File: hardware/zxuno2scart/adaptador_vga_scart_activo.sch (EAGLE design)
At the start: 13 parts, among them T1 2N3904, T2 2N3904, T3 2N3904

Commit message: 
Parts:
- C1, C3: device capacitor-wima:C5/3.5 -> capacitor-wima:C2,5-3
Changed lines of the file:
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@@
 <?xml version="1.0" encoding="utf-8"?>
 <!DOCTYPE eagle SYSTEM "eagle.dtd">
-<eagle version="6.5.0">
+<eagle version="7.3.0">
 <drawing>
 <settings>
@@
 <grid distance="0.1" unitdist="inch" unit="inch" style="lines" multiple="1" display="no" altdistance="0.01" altunitdist="inch" altunit="inch"/>
 <layers>
-<layer number="1" name="Top" color="4" fill="1" visible="no" active="no"/>
-<layer number="2" name="Route2" color="1" fill="3" visible="no" active="no"/>
-<layer number="3" name="Route3" color="4" fill="3" visible="no" active="no"/>
-<layer number="4" name="Route4" color="1" fill="4" visible="no" active="no"/>
-<layer number="5" name="Route5" color="4" fill="4" visible="no" active="no"/>
-<layer number="6" name="Route6" color="1" fill="8" visible="no" active="no"/>
-<layer number="7" name="Route7" color="4" fill="8" visible="no" active="no"/>
-<layer number="8" name="Route8" color="1" fill="2" visible="no" active="no"/>
-<layer number="9" name="Route9" color="4" fill="2" visible="no" active="no"/>
-<layer number="10" name="Route10" color="1" fill="7" visible="no" active="no"/>
-<layer number="11" name="Route11" color="4" fill="7" visible="no" active="no"/>
-<layer number="12" name="Route12" color="1" fill="5" visible="no" active="no"/>
-<layer number="13" name="Route13" color="4" fill="5" visible="no" active="no"/>
-<layer number="14" name="Route14" color="1" fill="6" visible="no" active="no"/>
-<layer number="15" name="Route15" color="4" fill="6" visible="no" active="no"/>
-<layer number="16" name="Bottom" color="1" fill="1" visible="no" active="no"/>
-<layer number="17" name="Pads" color="2" fill="1" visible="no" active="no"/>
-<layer number="18" name="Vias" color="2" fill="1" visible="no" active="no"/>
-<layer number="19" name="Unrouted" color="6" fill="1" visible="no" active="no"/>
-<layer number="20" name="Dimension" color="15" fill="1" visible="no" active="no"/>
-<layer number="21" name="tPlace" color="7" fill="1" visible="no" active="no"/>
-<layer number="22" name="bPlace" color="7" fill="1" visible="no" active="no"/>
-<layer number="23" name="tOrigins" color="15" fill="1" visible="no" active="no"/>
-<layer number="24" name="bOrigins" color="15" fill="1" visible="no" active="no"/>
-<layer number="25" name="tNames" color="7" fill="1" visible="no" active="no"/>
-<layer number="26" name="bNames" color="7" fill="1" visible="no" active="no"/>
-<layer number="27" name="tValues" color="7" fill="1" visible="no" active="no"/>
-<layer number="28" name="bValues" color="7" fill="1" visible="no" active="no"/>
+<layer number="1" name="Top" color="4" fill="1" visible="yes" active="no"/>
+<layer number="2" name="Route2" color="1" fill="3" visible="yes" active="no"/>
+<layer number="3" name="Route3" color="4" fill="3" visible="yes" active="no"/>
+<layer number="4" name="Route4" color="1" fill="4" visible="yes" active="no"/>
+<layer number="5" name="Route5" color="4" fill="4" visible="yes" active="no"/>
+<layer number="6" name="Route6" color="1" fill="8" visible="yes" active="no"/>
+<layer number="7" name="Route7" color="4" fill="8" visible="yes" active="no"/>
+<layer number="8" name="Route8" color="1" fill="2" visible="yes" active="no"/>
+<layer number="9" name="Route9" color="4" fill="2" visible="yes" active="no"/>
+<layer number="10" name="Route10" color="1" fill="7" visible="yes" active="no"/>
+<layer number="11" name="Route11" color="4" fill="7" visible="yes" active="no"/>
+<layer number="12" name="Route12" color="1" fill="5" visible="yes" active="no"/>
+<layer number="13" name="Route13" color="4" fill="5" visible="yes" active="no"/>
+<layer number="14" name="Route14" color="1" fill="6" visible="yes" active="no"/>
+<layer number="15" name="Route15" color="4" fill="6" visible="yes" active="no"/>
+<layer number="16" name="Bottom" color="1" fill="1" visible="yes" active="no"/>
+<layer number="17" name="Pads" color="2" fill="1" visible="yes" active="no"/>
+<layer number="18" name="Vias" color="2" fill="1" visible="yes" active="no"/>
+<layer number="19" name="Unrouted" color="6" fill="1" visible="yes" active="no"/>
+<layer number="20" name="Dimension" color="15" fill="1" visible="yes" active="no"/>
+<layer number="21" name="tPlace" color="7" fill="1" visible="yes" active="no"/>
+<layer number="22" name="bPlace" color="7" fill="1" visible="yes" active="no"/>
+<layer number="23" name="tOrigins" color="15" fill="1" visible="yes" active="no"/>
+<layer number="24" name="bOrigins" color="15" fill="1" visible="yes" active="no"/>
+<layer number="25" name="tNames" color="7" fill="1" visible="yes" active="no"/>
+<layer number="26" name="bNames" color="7" fill="1" visible="yes" active="no"/>
+<layer number="27" name="tValues" color="7" fill="1" visible="yes" active="no"/>
+<layer number="28" name="bValues" color="7" fill="1" visible="yes" active="no"/>
 <layer number="29" name="tStop" color="7" fill="3" visible="no" active="no"/>
 <layer number="30" name="bStop" color="7" fill="6" visible="no" active="no"/>
@@
 <layer number="35" name="tGlue" color="7" fill="4" visible="no" active="no"/>
 <layer number="36" name="bGlue" color="7" fill="5" visible="no" active="no"/>
-<layer number="37" name="tTest" color="7" fill="1" visible="no" active="no"/>
-<layer number="38" name="bTest" color="7" fill="1" visible="no" active="no"/>
+<layer number="37" name="tTest" color="7" fill="1" visible="yes" active="no"/>
+<layer number="38" name="bTest" color="7" fill="1" visible="yes" active="no"/>
 <layer number="39" name="tKeepout" color="4" fill="11" visible="no" active="no"/>
 <layer number="40" name="bKeepout" color="1" fill="11" visible="no" active="no"/>
@@
 <layer number="44" name="Drills" color="7" fill="1" visible="no" active="no"/>
 <layer number="45" name="Holes" color="7" fill="1" visible="no" active="no"/>
-<layer number="46" name="Milling" color="3" fill="1" visible="no" active="no"/>
-<layer number="47" name="Measures" color="7" fill="1" visible="no" active="no"/>
-<layer number="48" name="Document" color="7" fill="1" visible="no" active="no"/>
-<layer number="49" name="Reference" color="7" fill="1" visible="no" active="no"/>
-<layer number="50" name="dxf" color="7" fill="1" visible="no" active="no"/>
-<layer number="51" name="tDocu" color="7" fill="1" visible="no" active="no"/>
-<layer number="52" name="bDocu" color="7" fill="1" visible="no" active="no"/>
-<layer number="53" name="tGND_GNDA" color="7" fill="1" visible="no" active="no"/>
-<layer number="54" name="bGND_GNDA" color="7" fill="1" visible="no" active="no"/>
-<layer number="56" name="wert" color="7" fill="1" visible="no" active="no"/>
-<layer number="57" name="tCAD" color="7" fill="1" visible="no" active="no"/>
+<layer number="46" name="Milling" color="3" fill="1" visible="yes" active="no"/>
+<layer number="47" name="Measures" color="7" fill="1" visible="yes" active="no"/>
+<layer number="48" name="Document" color="7" fill="1" visible="yes" active="no"/>
+<layer number="49" name="Reference" color="7" fill="1" visible="yes" active="no"/>
+<layer number="50" name="dxf" color="7" fill="1" visible="yes" active="no"/>
+<layer number="51" name="tDocu" color="7" fill="1" visible="yes" active="no"/>
+<layer number="52" name="bDocu" color="7" fill="1" visible="yes" active="no"/>
+<layer number="53" name="tGND_GNDA" color="7" fill="1" visible="yes" active="no"/>
+<layer number="54" name="bGND_GNDA" color="7" fill="1" visible="yes" active="no"/>
+<layer number="56" name="wert" color="7" fill="1" visible="yes" active="no"/>
+<layer number="57" name="tCAD" color="7" fill="1" visible="yes" active="no"/>
 <layer number="90" name="Modules" color="7" fill="1" visible="yes" active="yes"/>
 <layer number="91" name="Nets" color="2" fill="1" visible="yes" active="yes"/>
@@
 <part name="L1" library="inductors" deviceset="BL0" device="1RN1A"/>
 <part name="P+1" library="supply1" deviceset="VCC" device=""/>
-<part name="C1" library="capacitor-wima" deviceset="C" device="5/3.5"/>
+<part name="C1" library="capacitor-wima" deviceset="C" device="2,5-3"/>
 <part name="C2" library="capacitor-wima" deviceset="C" device="5/3.5"/>
-<part name="C3" library="capacitor-wima" deviceset="C" device="5/3.5"/>
+<part name="C3" library="capacitor-wima" deviceset="C" device="2,5-3"/>
 <part name="GND3" library="supply1" deviceset="GND" device=""/>
 <part name="GND4" library="supply1" deviceset="GND" device=""/>

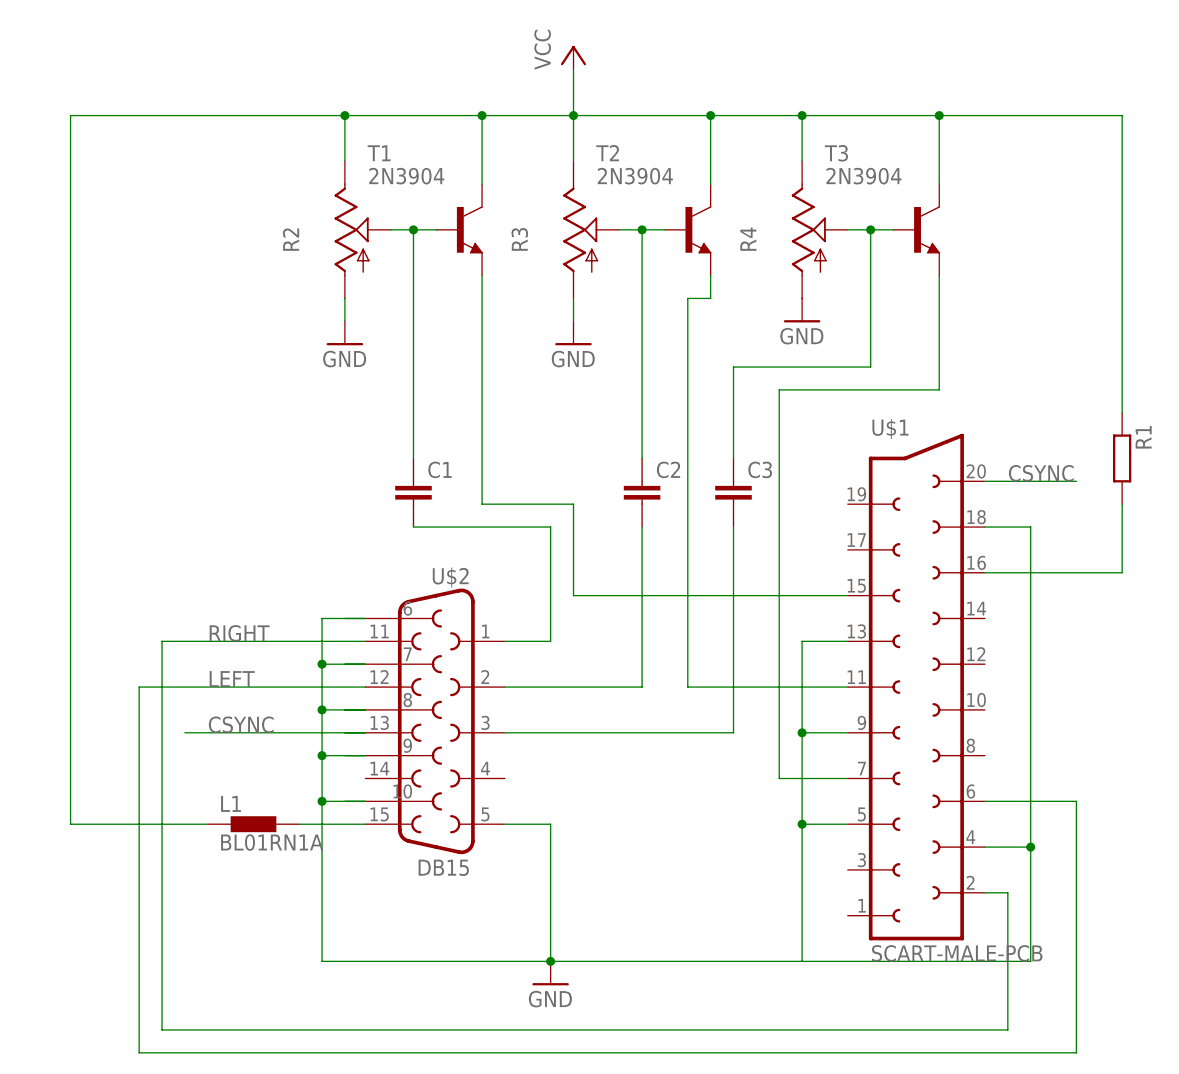
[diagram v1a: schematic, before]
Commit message: 
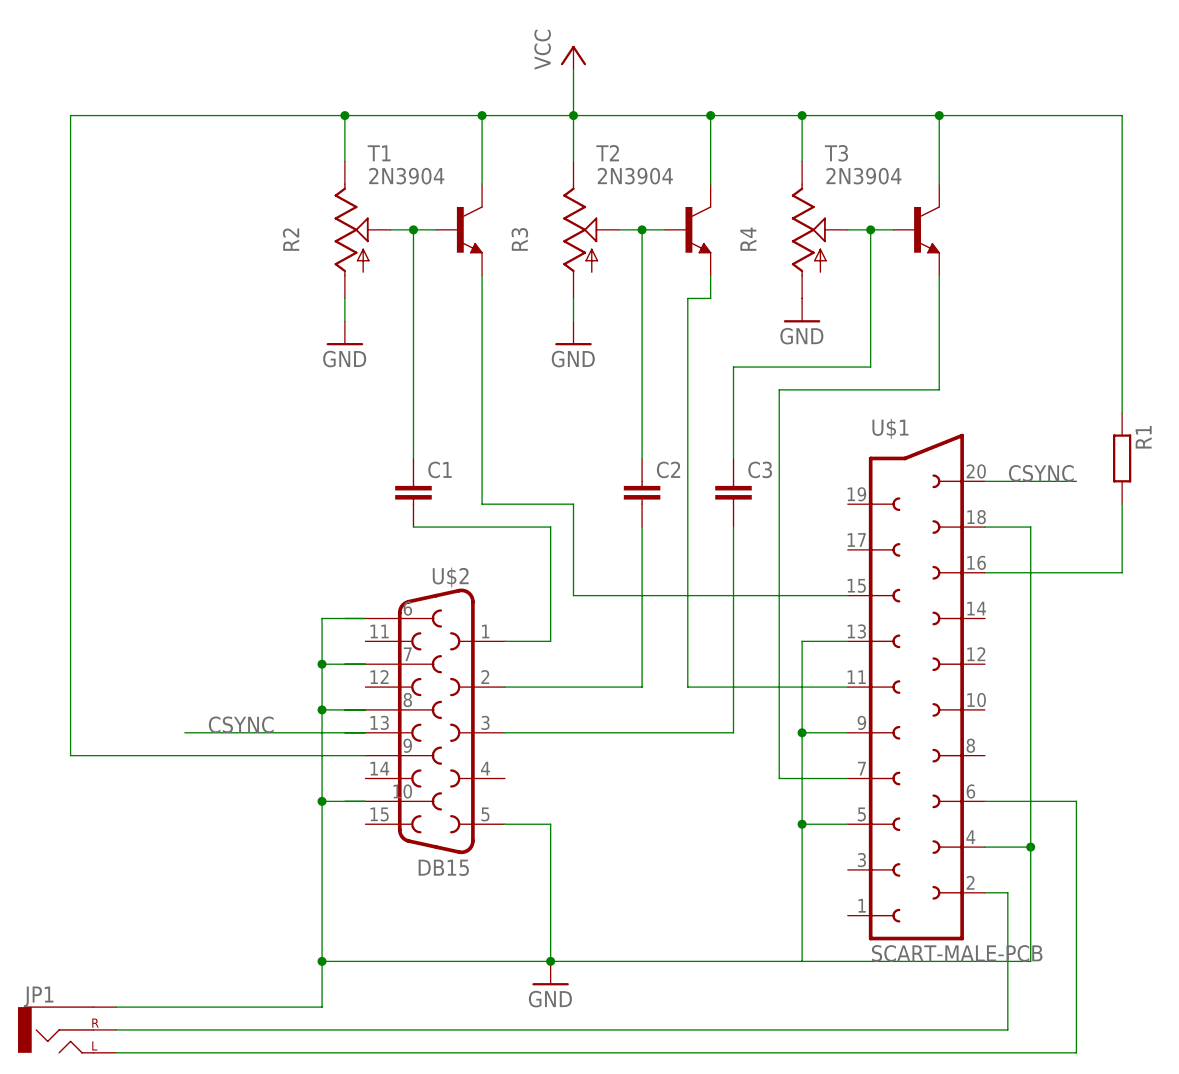
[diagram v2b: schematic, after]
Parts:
- removed L1: BL01RN1A, inductors:BL01RN1A
- added JP1: (no value), SparkFun-Connectors:AUDIO-JACKPTH
- C2: device capacitor-wima:C5/3.5 -> capacitor-wima:C2,5-3
- R1: device rcl:R-EU_0204/7 -> rcl:R-EU_0204/5
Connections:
- removed net N$2: L1.2, U$2.15
- net GND: now also JP1.SLEEVE; no longer U$2.9
- net LEFT: now also JP1.LEFT; no longer U$2.12
- net RIGHT: now also JP1.RIGHT; no longer U$2.11
- net VCC: now also U$2.9; no longer L1.1
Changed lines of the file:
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@@
 <layer number="113" name="IDFDebug" color="4" fill="1" visible="yes" active="yes"/>
 <layer number="116" name="Patch_BOT" color="7" fill="1" visible="yes" active="yes"/>
+<layer number="118" name="Rect_Pads" color="7" fill="1" visible="yes" active="yes"/>
 <layer number="121" name="_tsilk" color="7" fill="1" visible="yes" active="yes"/>
 <layer number="122" name="_bsilk" color="7" fill="1" visible="yes" active="yes"/>
@@
 <layer number="127" name="_tValues" color="7" fill="1" visible="yes" active="yes"/>
 <layer number="128" name="_bValues" color="7" fill="1" visible="yes" active="yes"/>
+<layer number="130" name="tSilk" color="7" fill="1" visible="yes" active="yes"/>
 <layer number="131" name="tAdjust" color="7" fill="1" visible="yes" active="yes"/>
 <layer number="132" name="bAdjust" color="7" fill="1" visible="yes" active="yes"/>
+<layer number="133" name="Ports" color="7" fill="1" visible="yes" active="yes"/>
+<layer number="134" name="Port2" color="7" fill="1" visible="yes" active="yes"/>
+<layer number="135" name="Port3" color="7" fill="1" visible="yes" active="yes"/>
 <layer number="144" name="Drill_legend" color="7" fill="1" visible="yes" active="yes"/>
 <layer number="150" name="Notes" color="7" fill="1" visible="yes" active="yes"/>
@@
 <layer number="223" name="223bmp" color="7" fill="1" visible="yes" active="yes"/>
 <layer number="224" name="224bmp" color="7" fill="1" visible="yes" active="yes"/>
+<layer number="231" name="Eagle3D_PG1" color="7" fill="1" visible="yes" active="yes"/>
+<layer number="232" name="Eagle3D_PG2" color="7" fill="1" visible="yes" active="yes"/>
+<layer number="233" name="Eagle3D_PG3" color="7" fill="1" visible="yes" active="yes"/>
 <layer number="248" name="Housing" color="7" fill="1" visible="yes" active="yes"/>
 <layer number="249" name="Edge" color="7" fill="1" visible="yes" active="yes"/>
@@
 <part name="U$1" library="con-hirschmann" deviceset="SCART-MALE-PCB" device=""/>
 <part name="U$2" library="SparkFun-Connectors" deviceset="DB15" device=""/>
-<part name="R1" library="rcl" deviceset="R-EU_" device="0204/7"/>
+<part name="R1" library="rcl" deviceset="R-EU_" device="0204/5"/>
 <part name="T1" library="transistor" deviceset="2N3904" device=""/>
 <part name="T2" library="transistor" deviceset="2N3904" device=""/>
@@
 <part name="GND1" library="supply1" deviceset="GND" device=""/>
 <part name="GND2" library="supply1" deviceset="GND" device=""/>
-<part name="L1" library="inductors" deviceset="BL0" device="1RN1A"/>
 <part name="P+1" library="supply1" deviceset="VCC" device=""/>
 <part name="C1" library="capacitor-wima" deviceset="C" device="2,5-3"/>
-<part name="C2" library="capacitor-wima" deviceset="C" device="5/3.5"/>
+<part name="C2" library="capacitor-wima" deviceset="C" device="2,5-3"/>
 <part name="C3" library="capacitor-wima" deviceset="C" device="2,5-3"/>
 <part name="GND3" library="supply1" deviceset="GND" device=""/>
@@
 <part name="R3" library="pot" deviceset="TRIM_US-" device="CA6V"/>
 <part name="R4" library="pot" deviceset="TRIM_US-" device="CA6V"/>
+<part name="JP1" library="SparkFun-Connectors" deviceset="AUDIO-JACK" device="PTH"/>
 </parts>
 <sheets>
@@
 <instance part="GND1" gate="1" x="-15.24" y="17.78"/>
 <instance part="GND2" gate="1" x="-12.7" y="88.9"/>
-<instance part="L1" gate="G$1" x="-48.26" y="35.56"/>
 <instance part="P+1" gate="VCC" x="-12.7" y="121.92"/>
 <instance part="C1" gate="G$1" x="-30.48" y="73.66"/>
@@
 <instance part="R3" gate="G$1" x="-12.7" y="101.6"/>
 <instance part="R4" gate="G$1" x="12.7" y="101.6"/>
+<instance part="JP1" gate="G$1" x="-68.58" y="12.7"/>
 </instances>
 <busses>
@@
 <wire x1="-15.24" y1="20.32" x2="-40.64" y2="20.32" width="0.1524" layer="91"/>
 <wire x1="-40.64" y1="20.32" x2="-40.64" y2="38.1" width="0.1524" layer="91"/>
-<wire x1="-40.64" y1="38.1" x2="-40.64" y2="43.18" width="0.1524" layer="91"/>
-<wire x1="-40.64" y1="43.18" x2="-40.64" y2="48.26" width="0.1524" layer="91"/>
+<wire x1="-40.64" y1="38.1" x2="-40.64" y2="48.26" width="0.1524" layer="91"/>
 <wire x1="-40.64" y1="48.26" x2="-40.64" y2="53.34" width="0.1524" layer="91"/>
 <wire x1="-40.64" y1="53.34" x2="-40.64" y2="58.42" width="0.1524" layer="91"/>
@@
 <wire x1="-38.1" y1="48.26" x2="-35.814" y2="48.26" width="0.1524" layer="91"/>
 <wire x1="-35.814" y1="48.26" x2="-40.64" y2="48.26" width="0.1524" layer="91"/>
-<wire x1="-38.1" y1="43.18" x2="-35.814" y2="43.18" width="0.1524" layer="91"/>
-<wire x1="-35.814" y1="43.18" x2="-40.64" y2="43.18" width="0.1524" layer="91"/>
 <wire x1="-38.1" y1="38.1" x2="-35.814" y2="38.1" width="0.1524" layer="91"/>
 <junction x="-40.64" y="53.34"/>
 <junction x="-40.64" y="48.26"/>
-<junction x="-40.64" y="43.18"/>
 <junction x="-40.64" y="38.1"/>
 <wire x1="-35.814" y1="38.1" x2="-40.64" y2="38.1" width="0.1524" layer="91"/>
@@
 <pinref part="U$2" gate="G$1" pin="7"/>
 <pinref part="U$2" gate="G$1" pin="8"/>
-<pinref part="U$2" gate="G$1" pin="9"/>
 <pinref part="U$2" gate="G$1" pin="10"/>
 <pinref part="U$2" gate="G$1" pin="6"/>
 <pinref part="GND1" gate="1" pin="GND"/>
+<pinref part="JP1" gate="G$1" pin="SLEEVE"/>
+<wire x1="-63.5" y1="15.24" x2="-40.64" y2="15.24" width="0.1524" layer="91"/>
+<wire x1="-40.64" y1="15.24" x2="-40.64" y2="20.32" width="0.1524" layer="91"/>
+<junction x="-40.64" y="20.32"/>
 </segment>
 <segment>
@@
 <net name="LEFT" class="0">
 <segment>
-<wire x1="-60.96" y1="50.8" x2="-60.96" y2="10.16" width="0.1524" layer="91"/>
-<wire x1="-60.96" y1="10.16" x2="43.18" y2="10.16" width="0.1524" layer="91"/>
+<wire x1="-63.5" y1="10.16" x2="43.18" y2="10.16" width="0.1524" layer="91"/>
 <wire x1="43.18" y1="10.16" x2="43.18" y2="38.1" width="0.1524" layer="91"/>
 <pinref part="U$1" gate="G$1" pin="6"/>
 <wire x1="43.18" y1="38.1" x2="33.02" y2="38.1" width="0.1524" layer="91"/>
-<pinref part="U$2" gate="G$1" pin="12"/>
-<wire x1="-35.814" y1="50.8" x2="-60.96" y2="50.8" width="0.1524" layer="91"/>
-<label x="-53.34" y="50.8" size="1.778" layer="95"/>
+<pinref part="JP1" gate="G$1" pin="LEFT"/>
 </segment>
 </net>
 <net name="RIGHT" class="0">
 <segment>
-<wire x1="-58.42" y1="55.88" x2="-58.42" y2="12.7" width="0.1524" layer="91"/>
-<wire x1="-58.42" y1="12.7" x2="35.56" y2="12.7" width="0.1524" layer="91"/>
+<wire x1="-63.5" y1="12.7" x2="35.56" y2="12.7" width="0.1524" layer="91"/>
 <pinref part="U$1" gate="G$1" pin="2"/>
 <wire x1="35.56" y1="12.7" x2="35.56" y2="27.94" width="0.1524" layer="91"/>
 <wire x1="35.56" y1="27.94" x2="33.02" y2="27.94" width="0.1524" layer="91"/>
-<pinref part="U$2" gate="G$1" pin="11"/>
-<wire x1="-58.42" y1="55.88" x2="-35.814" y2="55.88" width="0.1524" layer="91"/>
-<label x="-53.34" y="55.88" size="1.778" layer="95"/>
+<pinref part="JP1" gate="G$1" pin="RIGHT"/>
 </segment>
 </net>
@@
 <wire x1="33.02" y1="73.66" x2="43.18" y2="73.66" width="0.1524" layer="91"/>
 <label x="35.56" y="73.66" size="1.778" layer="95"/>
-</segment>
-</net>
-<net name="N$2" class="0">
-<segment>
-<pinref part="U$2" gate="G$1" pin="15"/>
-<pinref part="L1" gate="G$1" pin="2"/>
-<wire x1="-35.814" y1="35.56" x2="-43.18" y2="35.56" width="0.1524" layer="91"/>
 </segment>
 </net>
@@
 <net name="VCC" class="0">
 <segment>
-<wire x1="-68.58" y1="35.56" x2="-68.58" y2="114.3" width="0.1524" layer="91"/>
+<wire x1="-68.58" y1="43.18" x2="-68.58" y2="114.3" width="0.1524" layer="91"/>
 <wire x1="-68.58" y1="114.3" x2="-38.1" y2="114.3" width="0.1524" layer="91"/>
-<pinref part="L1" gate="G$1" pin="1"/>
 <wire x1="-38.1" y1="114.3" x2="-22.86" y2="114.3" width="0.1524" layer="91"/>
 <wire x1="-22.86" y1="114.3" x2="-12.7" y2="114.3" width="0.1524" layer="91"/>
@@
 <wire x1="12.7" y1="114.3" x2="27.94" y2="114.3" width="0.1524" layer="91"/>
 <wire x1="27.94" y1="114.3" x2="48.26" y2="114.3" width="0.1524" layer="91"/>
-<wire x1="-53.34" y1="35.56" x2="-68.58" y2="35.56" width="0.1524" layer="91"/>
 <pinref part="P+1" gate="VCC" pin="VCC"/>
 <wire x1="-12.7" y1="119.38" x2="-12.7" y2="114.3" width="0.1524" layer="91"/>
@@
 <pinref part="R3" gate="G$1" pin="E"/>
 <pinref part="R4" gate="G$1" pin="E"/>
-</segment>
-</net>
+<pinref part="U$2" gate="G$1" pin="9"/>
+<wire x1="-35.814" y1="43.18" x2="-68.58" y2="43.18" width="0.1524" layer="91"/>
+</segment>
+</net>
